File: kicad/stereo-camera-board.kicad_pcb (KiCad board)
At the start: 4 copper layers, 57 x 70 mm, 153 parts, among them IC1 ZLDO1117G33TA, IC2 MCP1700T-2502E/TT, IC3 SN74LVC1T45DCKR, IC4 SN74LVC1T45DCKR, IC5 SN74LVC1T45DCKR, T1 2n2222a, T2 2N2907A, U1 GSB311231HR, U2 ATXMEGA256A3-AU, U3 MAX3207E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

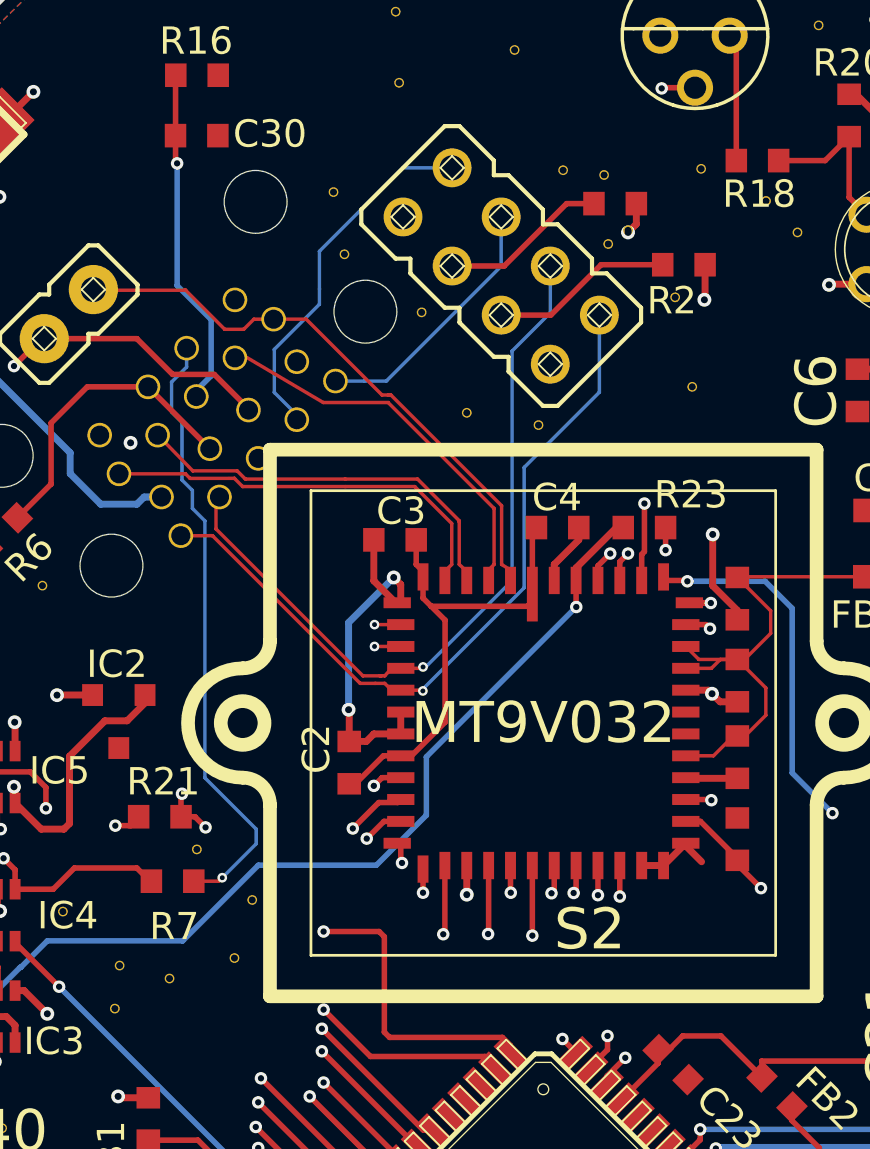
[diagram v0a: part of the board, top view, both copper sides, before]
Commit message: Rebuilt .net file Fixed errors in pcb due to misnamed module references
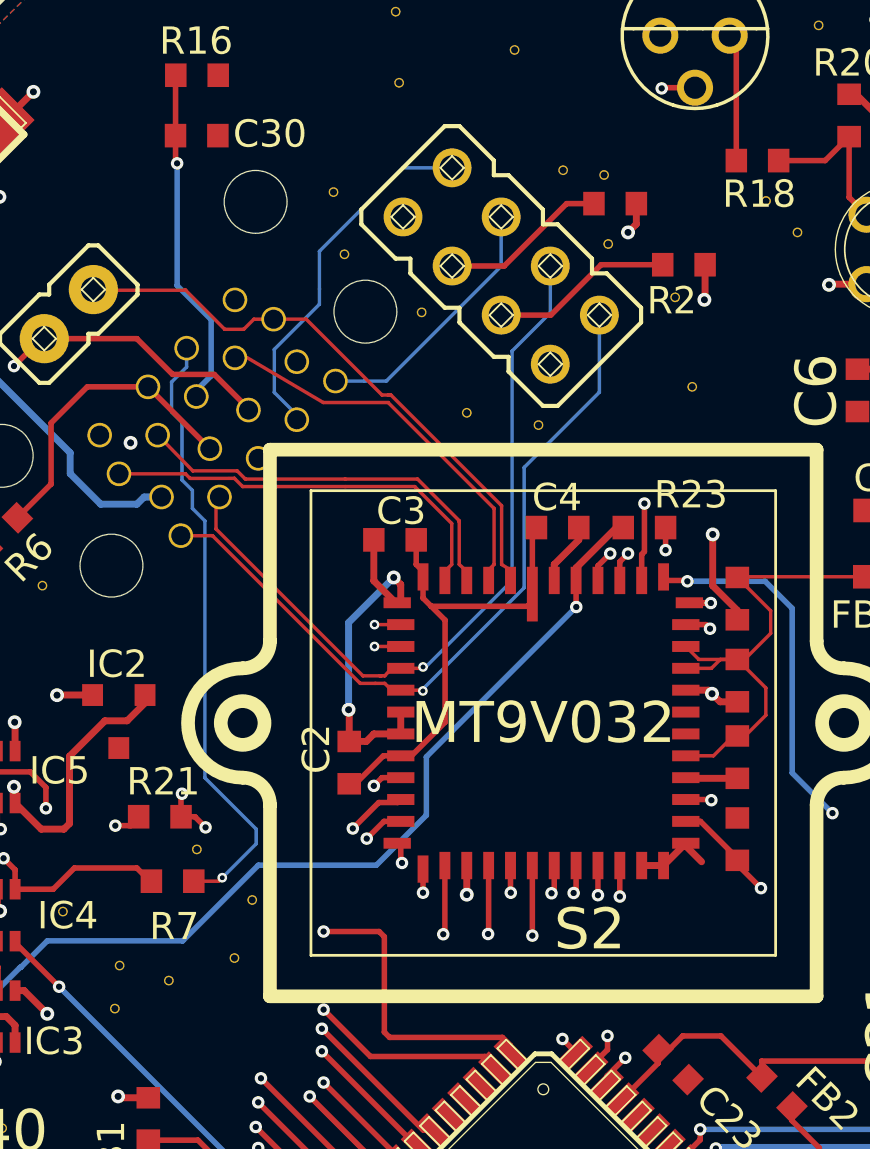
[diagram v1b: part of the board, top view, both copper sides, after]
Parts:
- removed the Via5Mil at (154.3, 87.5)
- removed the Via5Mil at (151.6, 89.7)
- P1: renamed from FSM4JSMA-SMD; value RESET -> FSM4JSMA-SMD
- moved Via5Mil 0.08 mm to (134.8, 117.2)
- renumbered PDI to PDIJTAG1
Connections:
- P1 pad P$4: N-0000090 -> Net-(JP3-Pad6)
- PDIJTAG1 pad 1: N-0000016 -> Net-(PDIJTAG1-Pad1)
- PDIJTAG1 pad 5: N-0000090 -> Net-(JP3-Pad6)
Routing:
- net Net-(JP3-Pad6): track 36.3 -> 64.8 mm, vias 2 -> 4
- net N-0000090: track 28.5 -> 0.00 mm, vias 2 -> 0
- net Net-(PDIJTAG1-Pad1): track 1.07 -> 21.3 mm, vias 0 -> 2
- net N-0000016: track 20.3 -> 0.00 mm, vias 2 -> 0

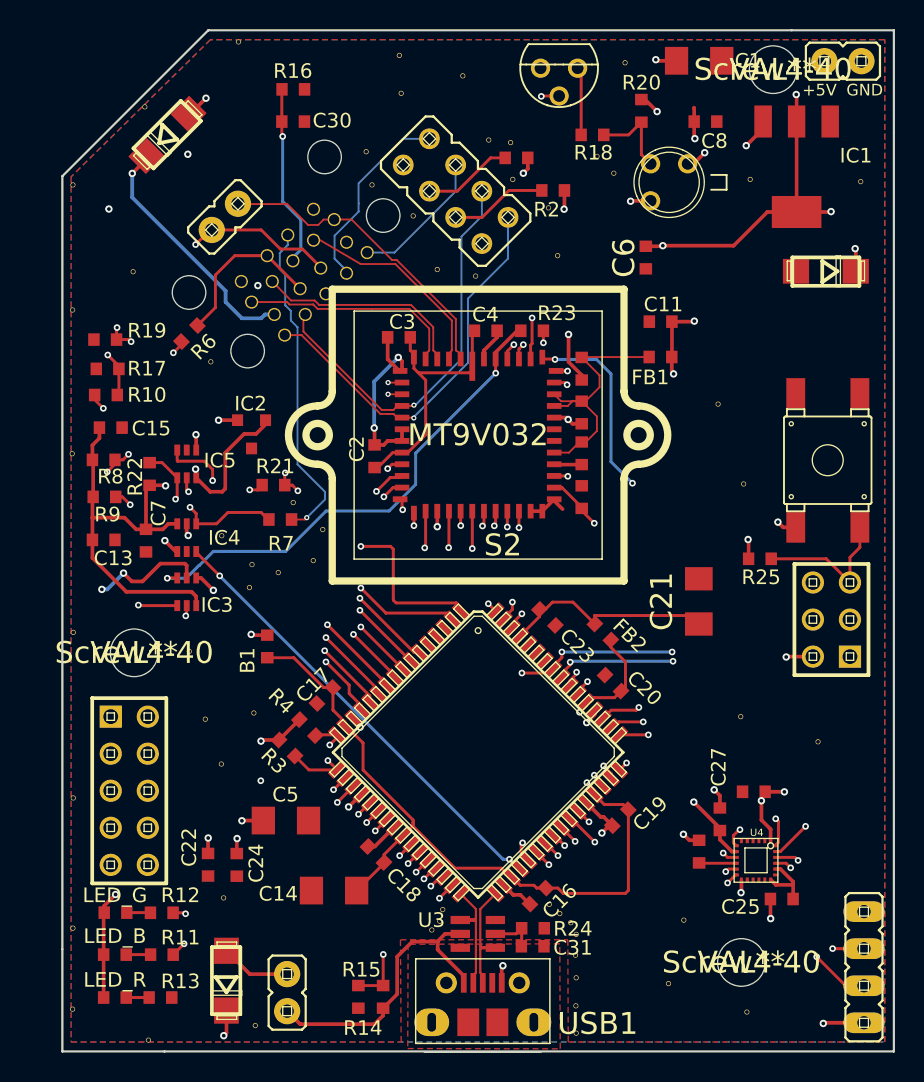
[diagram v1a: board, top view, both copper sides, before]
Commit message: Fixed unconnected nets
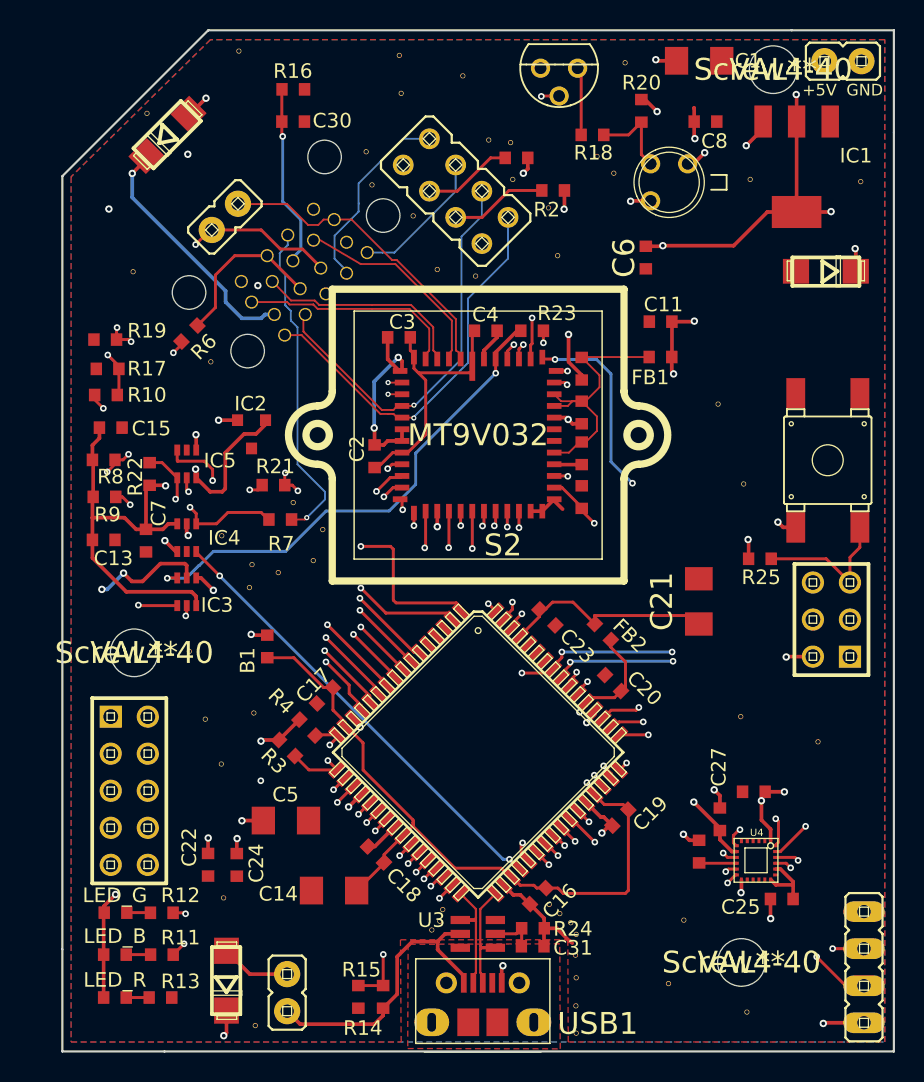
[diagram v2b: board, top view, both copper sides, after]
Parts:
- removed the Via5Mil at (125.9, 149.2)
- removed the Via5Mil at (120.7, 147.1)
- removed the Via5Mil at (120.7, 141.6)
- removed the Via5Mil at (120.8, 132.6)
- removed the Via5Mil at (120.8, 121.3)
- removed the Via5Mil at (120.7, 109.0)
- removed the Via5Mil at (120.7, 99.2)
- removed the Via5Mil at (120.7, 90.6)
- moved Via5Mil 0.63 mm to (132.1, 81.4)
- moved Via5Mil 0.47 mm to (125.8, 85.7)
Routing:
- net GND: track 53.9 -> 59.6 mm

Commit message: Added gerber folder and plotted gerber and drill files. Fixed some silk screen objects.
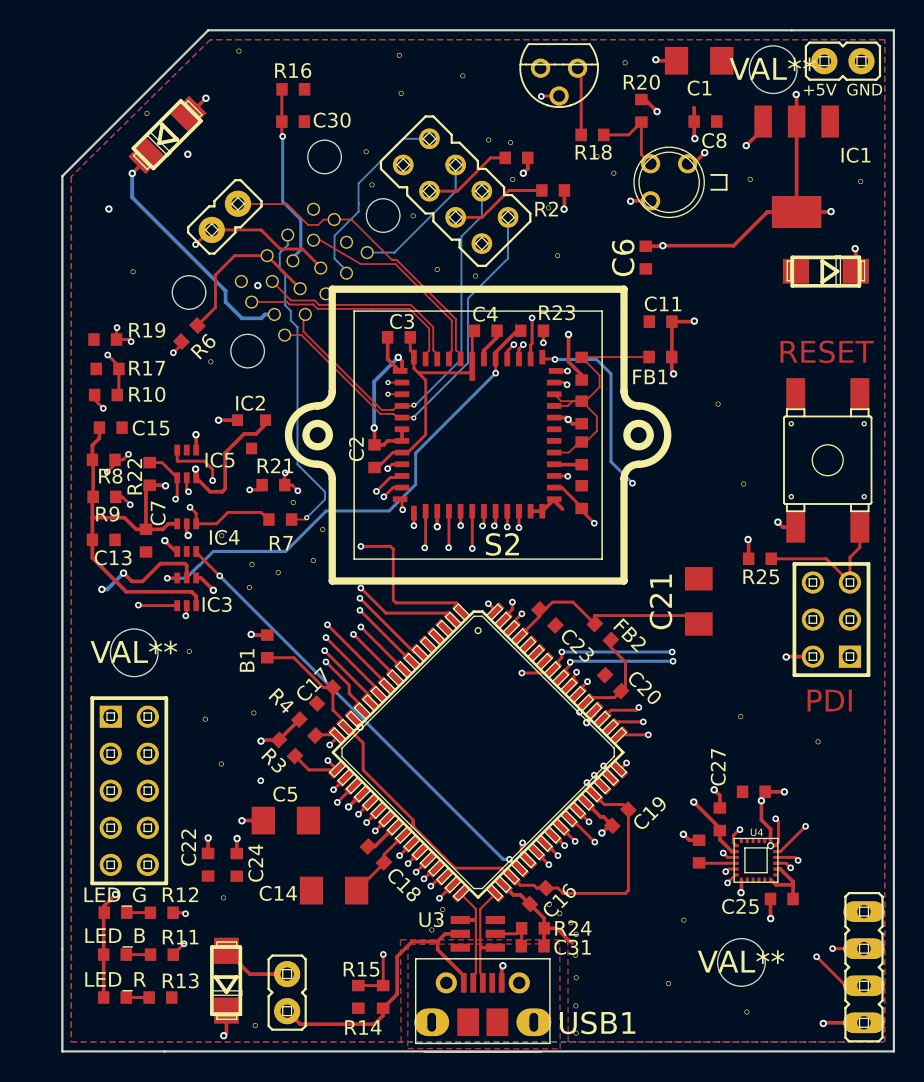
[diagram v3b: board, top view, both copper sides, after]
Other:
- board text added: "PDI"
- board text added: "RESET"
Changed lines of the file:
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@@
     (links 254)
     (no_connects 0)
-    (area 119.924999 79.924999 177.075001 150.075001)
+    (area 107.779144 64.798058 193.236213 155.002)
     (thickness 1.6)
-    (drawings 11)
+    (drawings 13)
     (tracks 1191)
     (zones 0)
@@
   (layers
     (15 F.Cu power)
-    (2 Inner2.Cu mixed hide)
-    (1 Inner1.Cu mixed hide)
-    (0 B.Cu power hide)
+    (2 Inner2.Cu mixed)
+    (1 Inner1.Cu mixed)
+    (0 B.Cu power)
     (16 B.Adhes user)
     (17 F.Adhes user)
@@
   (module SMD-1206 (layer F.Cu)
     (at 163.6522 82.0928)
-    (fp_text reference C1 (at 3.3478 0.0072) (layer F.SilkS)
+    (fp_text reference C1 (at 0.0478 1.9072) (layer F.SilkS)
       (effects (font (size 1 1) (thickness 0.15)))
     )
@@
       (effects (font (size 1.5 1.5) (thickness 0.15)))
     )
-    (fp_text value MT9V032 (at 0 0) (layer F.SilkS)
+    (fp_text value MT9V032 (at 0 0) (layer F.SilkS) hide
       (effects (font (size 1.5 1.5) (thickness 0.15)))
     )
@@
   (module ViasAndHoles:Screw4-40 (layer F.Cu)
     (at 166.55 143.9)
-    (fp_text reference Screw4-40 (at 0 0) (layer F.SilkS)
+    (fp_text reference Screw4-40 (at 0 0) (layer F.SilkS) hide
       (effects (font (size 1.5 1.5) (thickness 0.15)))
     )
@@
   (module ViasAndHoles:Screw4-40 (layer F.Cu)
     (at 168.725 82.7)
-    (fp_text reference Screw4-40 (at 0 0) (layer F.SilkS)
+    (fp_text reference Screw4-40 (at 0 0) (layer F.SilkS) hide
       (effects (font (size 1.5 1.5) (thickness 0.15)))
     )
@@
   (module ViasAndHoles:Screw4-40 (layer F.Cu)
     (at 124.925 122.675)
-    (fp_text reference Screw4-40 (at 0 0) (layer F.SilkS)
+    (fp_text reference Screw4-40 (at 0 0) (layer F.SilkS) hide
       (effects (font (size 1.5 1.5) (thickness 0.15)))
     )
@@
       (clearance 0.006))
   )
+  (gr_text "PDI\n" (at 172.6 126) (layer F.Cu)
+    (effects (font (size 1.5 1.5) (thickness 0.3)))
+  )
+  (gr_text "RESET\n" (at 172.325 102.1) (layer F.Cu)
+    (effects (font (size 1.5 1.5) (thickness 0.3)))
+  )
   (gr_text GND (at 175 84.1) (layer F.SilkS)
     (effects (font (size 0.8 0.8) (thickness 0.15)))
@@
   (segment (start 159.9435 84.7468) (end 160.7693 85.5726) (width 0.254) (layer F.Cu) (net 3))
   (via (at 160.7693 85.5726) (size 0.508) (layers F.Cu B.Cu) (net 3))
-  (segment (start 153.035 141.56) (end 153.885 141.56) (width 0.254) (layer F.Cu) (net 4) (status 400000))
+  (segment (start 153.035 141.56) (end 153.885 141.56) (width 0.254) (layer F.Cu) (net 4))
   (segment (start 154.825 142.45) (end 154.95 142.575) (width 0.254) (layer F.Cu) (net 4))
   (segment (start 154.775 142.45) (end 154.825 142.45) (width 0.254) (layer F.Cu) (net 4))
   (segment (start 153.885 141.56) (end 154.775 142.45) (width 0.254) (layer F.Cu) (net 4))
-  (segment (start 153.015 142.79) (end 153.015 141.58) (width 0.254) (layer F.Cu) (net 4) (status C00000))
-  (segment (start 153.015 141.58) (end 153.025 141.57) (width 0.254) (layer F.Cu) (net 4) (status C00000))
-  (segment (start 153.025 141.57) (end 153.025 140.871016) (width 0.254) (layer F.Cu) (net 4) (status 400000))
-  (segment (start 153.025 140.871016) (end 152.051992 139.898008) (width 0.254) (layer F.Cu) (net 4) (status 800000))
+  (segment (start 153.015 142.79) (end 153.015 141.58) (width 0.254) (layer F.Cu) (net 4))
+  (segment (start 153.015 141.58) (end 153.025 141.57) (width 0.254) (layer F.Cu) (net 4))
+  (segment (start 153.025 141.57) (end 153.025 140.871016) (width 0.254) (layer F.Cu) (net 4))
+  (segment (start 153.025 140.871016) (end 152.051992 139.898008) (width 0.254) (layer F.Cu) (net 4))
   (segment (start 150.12 145.3) (end 150.12 144.205) (width 0.254) (layer F.Cu) (net 4))
   (via (at 150.2 144.125) (size 0.508) (layers F.Cu B.Cu) (net 4))
